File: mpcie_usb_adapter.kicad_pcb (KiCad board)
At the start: 2 copper layers, 85 x 56 mm, 23 parts, among them J1 USB4105-GF-A, J2 SMA-J-P-H-ST-EM1, J3 SMA-J-P-H-ST-EM1, J4 Conn_Coaxial_Small, J5 Conn_Coaxial_Small, U1 LD1117S33TR, U2 AS-RTK2B-MPCIE-L1L2-F9P-01

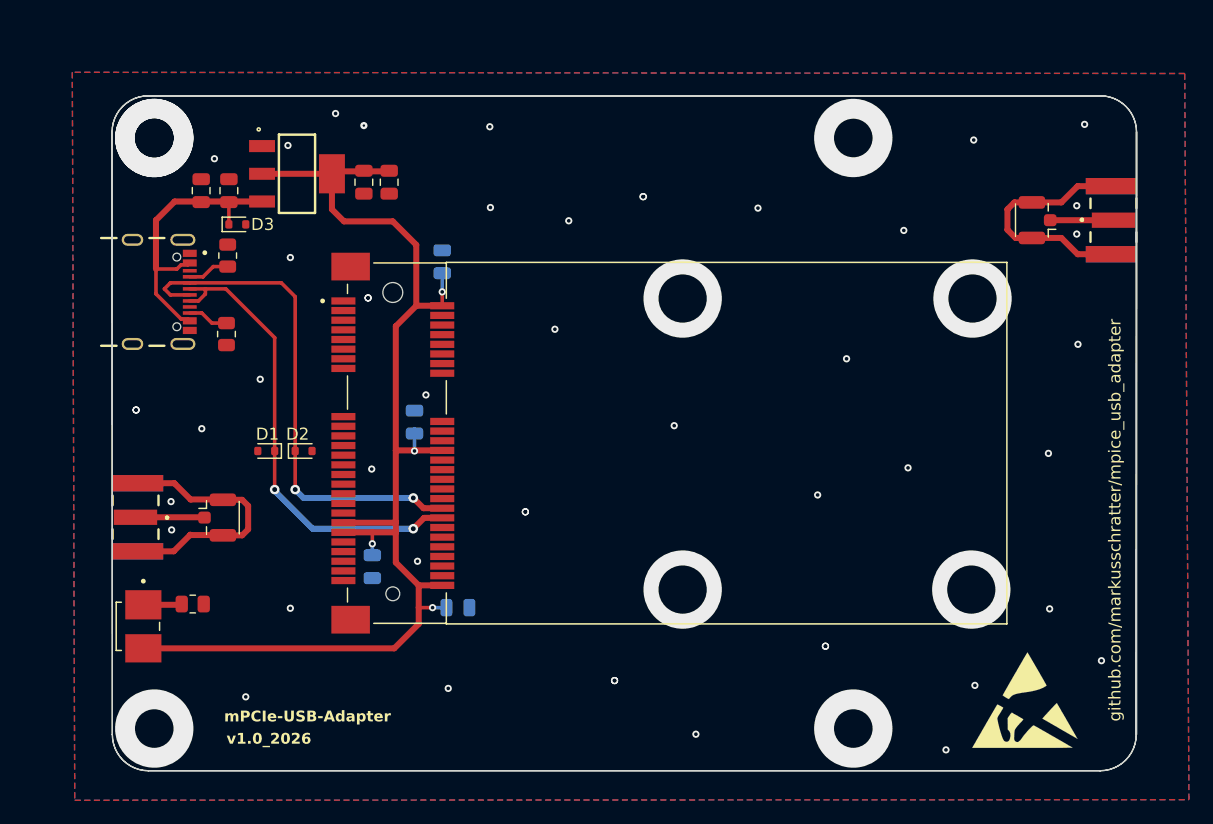
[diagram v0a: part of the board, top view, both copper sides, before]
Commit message: integrated updates from Matteo and added 3d models
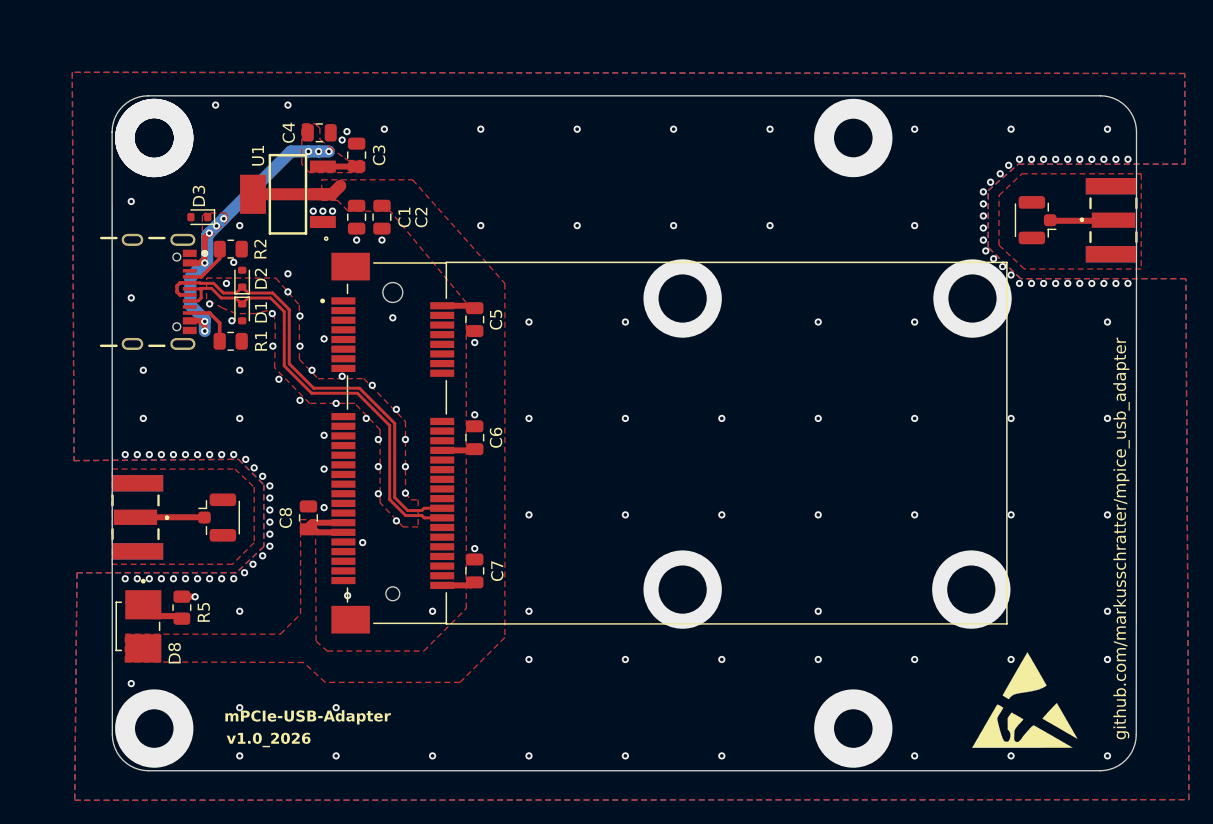
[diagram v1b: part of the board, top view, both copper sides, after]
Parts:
- C5, C6, C7, C8: moved to F.Cu
- moved D2 15.2 mm to (180.2, 80.4), turned to 90 degrees
- moved C3 13.2 mm to (189.7, 70.2)
- moved D1 11.7 mm to (180.2, 83.2), turned to -90 degrees
- moved C4 8.90 mm to (186.6, 68.3), turned to 0 degrees
- moved C8 6.67 mm to (185.7, 100.2), turned to 90 degrees
- moved C5 5.51 mm to (199.5, 83.8), turned to -90 degrees
- moved C6 5.17 mm to (199.5, 93.6)
- moved C7 3.36 mm to (199.5, 104.7), turned to 90 degrees
- moved D3 3.21 mm to (176.7, 75.3), turned to 180 degrees
- moved C1 2.96 mm to (189.7, 75.3)
- moved C2 2.96 mm to (191.8, 75.3)
- moved U1 1.86 mm to (184.0, 73.4), turned to 180 degrees
- moved R5 0.95 mm to (175.2, 107.7), turned to 90 degrees
- moved R1 0.69 mm to (179.2, 85.6), turned to 0 degrees
- moved R2 0.59 mm to (179.2, 78.0), turned to 0 degrees
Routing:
- net +3.3V: track 103.2 -> 22.0 mm, vias 4 -> 0
- net Net-(J4-Ext): track 21.4 -> 0.00 mm
- net Net-(J5-Ext): track 20.5 -> 0.00 mm
- net +5V: track 24.5 -> 35.3 mm, vias 0 -> 10
- net USB_D-: track 42.8 -> 38.3 mm, vias 2 -> 0
- net USB_D+: track 39.1 -> 37.4 mm, vias 2 -> 0
- net GND: track 0.00 -> 1.11 mm, vias 52 -> 176
- net Net-(J1-CC2): track 3.39 -> 4.34 mm
- added copper zone on F.Cu, net +3.3V
- added copper zone on F.Cu, net +5V
- added copper zone on F.Cu, net Net-(J4-Ext)
- added copper zone on F.Cu, net Net-(J5-Ext)
